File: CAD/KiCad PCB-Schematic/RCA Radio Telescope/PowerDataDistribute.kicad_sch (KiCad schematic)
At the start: 20 parts, among them J7 USB_A, J8 USB_A, Q1 DMP2008UFG-7, U13 MIC23050-SYML-TR, U14 TPS62133RGTR

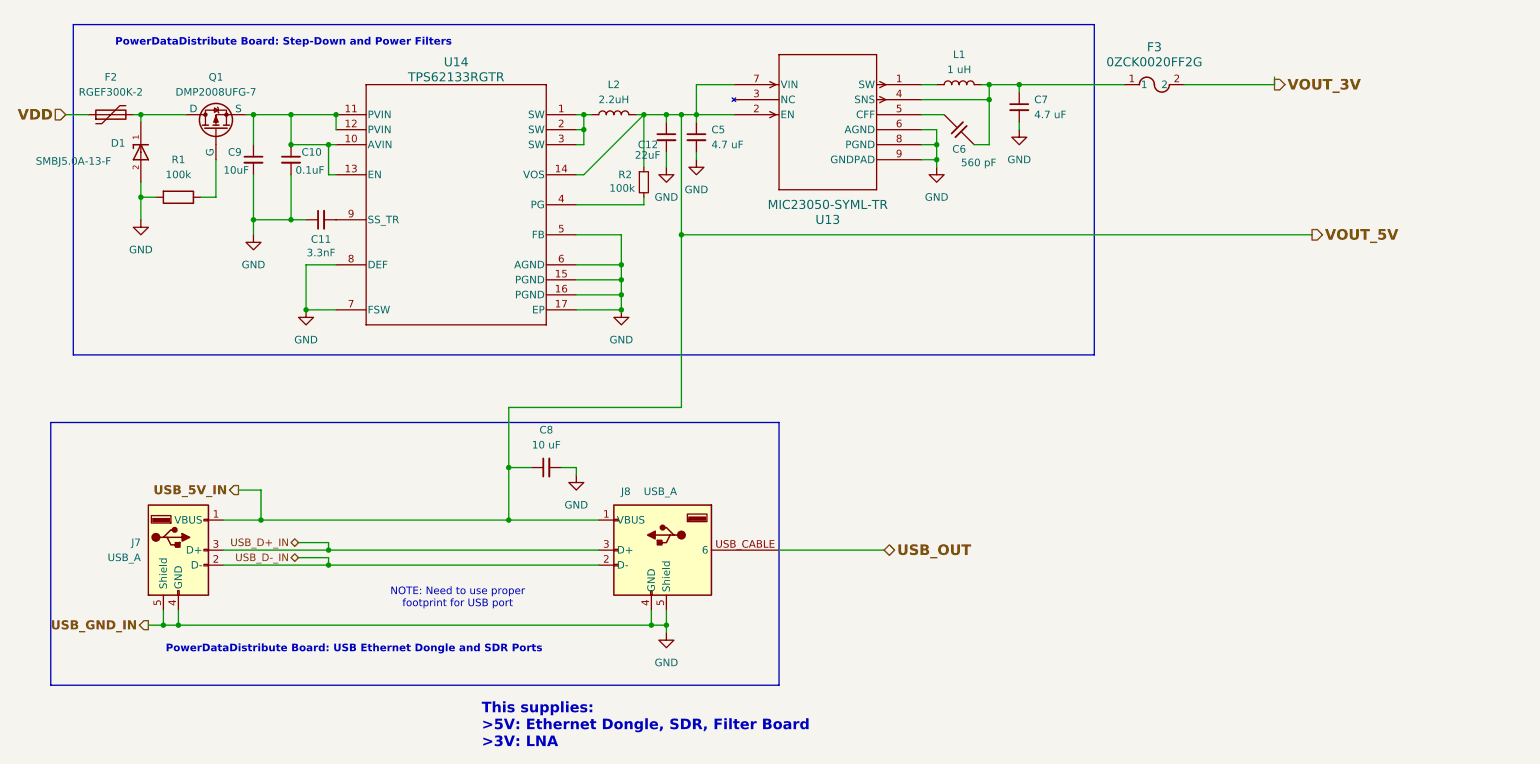
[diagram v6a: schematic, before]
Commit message: Updated Power/Data Schematic to v1.6 and Power/Data PCB to v1.5
- Added Testpoints to both Schematic and PCB
- Rearranged components on PCB to fit missing diode
- Changed Zener diode and PMOS on Protection Circuit to work with 12V max
- Fixed warnings and errors from DRC
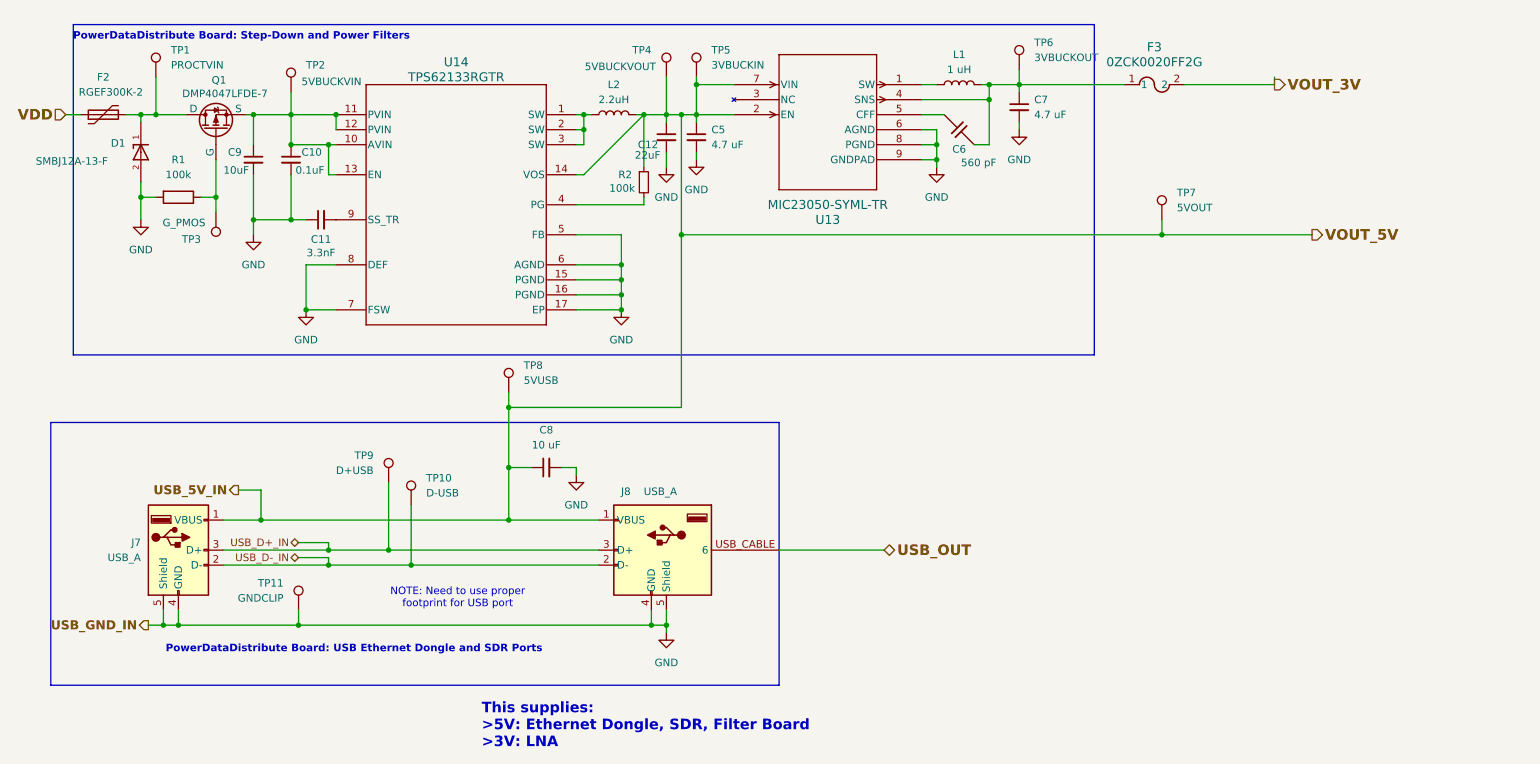
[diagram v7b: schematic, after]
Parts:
- added TP1: PROCTVIN, TestPoint:TestPoint_Pad_D1.0mm, symbol Connector:TestPoint
- added TP10: D-USB, TestPoint:TestPoint_Pad_D1.0mm, symbol Connector:TestPoint
- added TP11: GNDCLIP, TestPoint:TestPoint_Pad_4.0x4.0mm, symbol Connector:TestPoint
- added TP2: 5VBUCKVIN, TestPoint:TestPoint_Pad_D1.0mm, symbol Connector:TestPoint
- added TP3: G_PMOS, TestPoint:TestPoint_Pad_D1.0mm, symbol Connector:TestPoint
- added TP4: 5VBUCKVOUT, TestPoint:TestPoint_Pad_D1.0mm, symbol Connector:TestPoint
- added TP5: 3VBUCKIN, TestPoint:TestPoint_Pad_D1.0mm, symbol Connector:TestPoint
- added TP6: 3VBUCKOUT, TestPoint:TestPoint_Pad_D1.0mm, symbol Connector:TestPoint
- added TP7: 5VOUT, TestPoint:TestPoint_Pad_D1.0mm, symbol Connector:TestPoint
- added TP8: 5VUSB, TestPoint:TestPoint_Pad_D1.0mm, symbol Connector:TestPoint
- added TP9: D+USB, TestPoint:TestPoint_Pad_D1.0mm, symbol Connector:TestPoint
- D1: value SMBJ5.0A-13-F -> SMBJ12A-13-F; footprint SMBJ5.0A-13-F:DIOM5336X250N -> Library:SMB_DIO
- Q1: value DMP2008UFG-7 -> DMP4047LFDE-7; footprint Library:DMP2008UFG-7_DIO -> Library:U-DFN2020-6_DIO
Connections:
- net GND: now also TP11.1
- net USB_5V_IN: now also TP4.1, TP5.1, TP7.1, TP8.1
- net USB_D+_IN: now also TP9.1
- net USB_D-_IN: now also TP10.1
- net at D1.1, F2.2, Q1.1 (D): now also TP1.1
- net at C6.1, C7.1, F3.1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: now also TP6.1
- net at Q1.2 (G), R1.1: now also TP3.1
- net at C10.1, C9.1, Q1.3 (S)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: now also TP2.1
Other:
- moved on the sheet: F2

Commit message: Updated PowerData PCB to v1.6 and PowerData Schematic to v1.7
- Design Review with Andrew
- Fixed up various parts of PCB parameters
- May consider LDO or filtering for Power IC
- May want to consider a circuit breaker IC for LNA supply
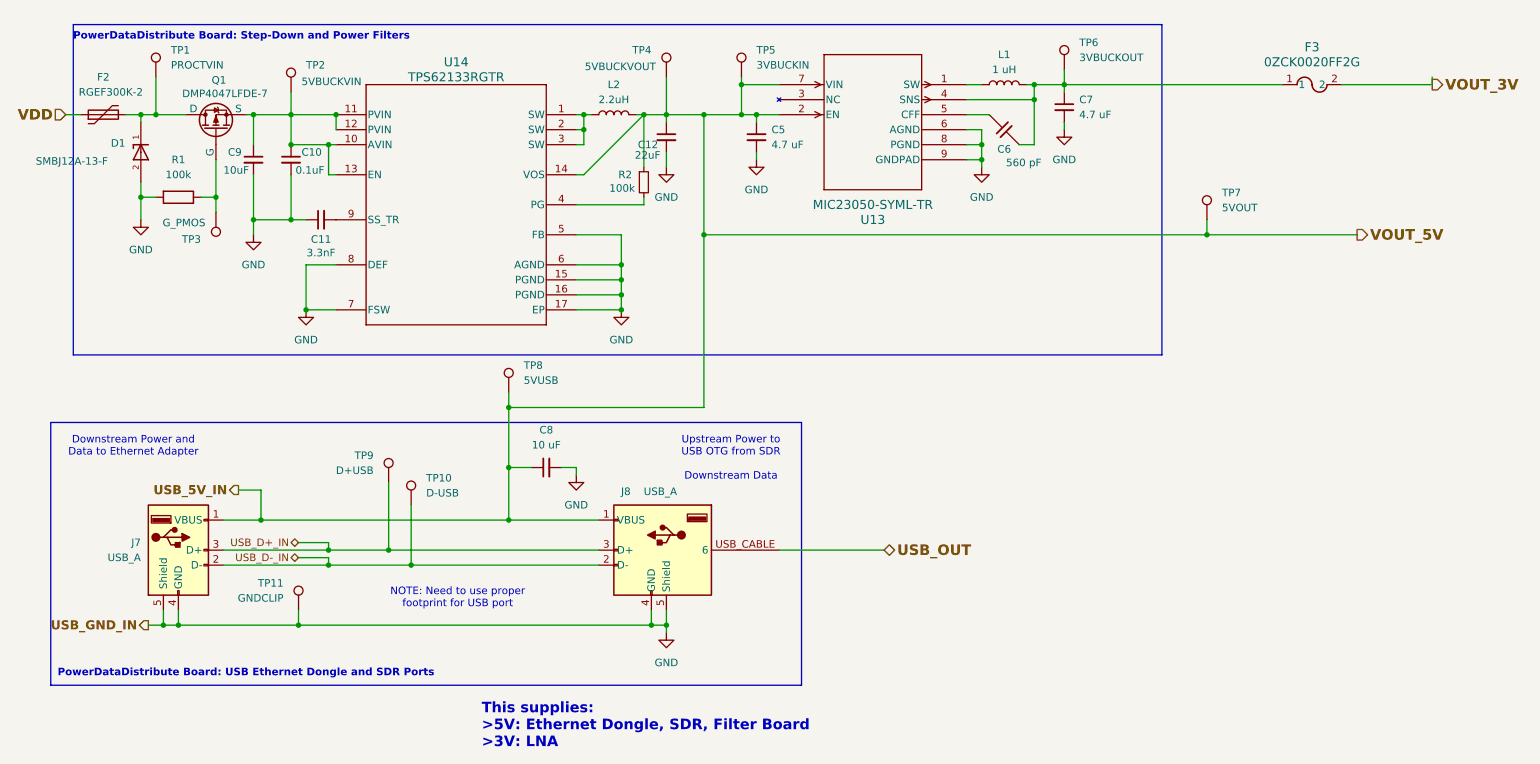
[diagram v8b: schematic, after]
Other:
- note added: "Downstream Power and Data to Ethernet Adapter"
- note added: "Upstream Power to USB OTG from SDR Downstream Data"
- moved on the sheet: C5, C6, C7, F3, L1, TP5, TP6, TP7, U13
